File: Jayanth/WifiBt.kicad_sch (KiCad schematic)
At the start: 34 parts, among them J1 Bus_M.2_1-2199230-6, J3 Bus_M.2_2199230-6, Y2 Oscillator_32.768kHz_ECS_2520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

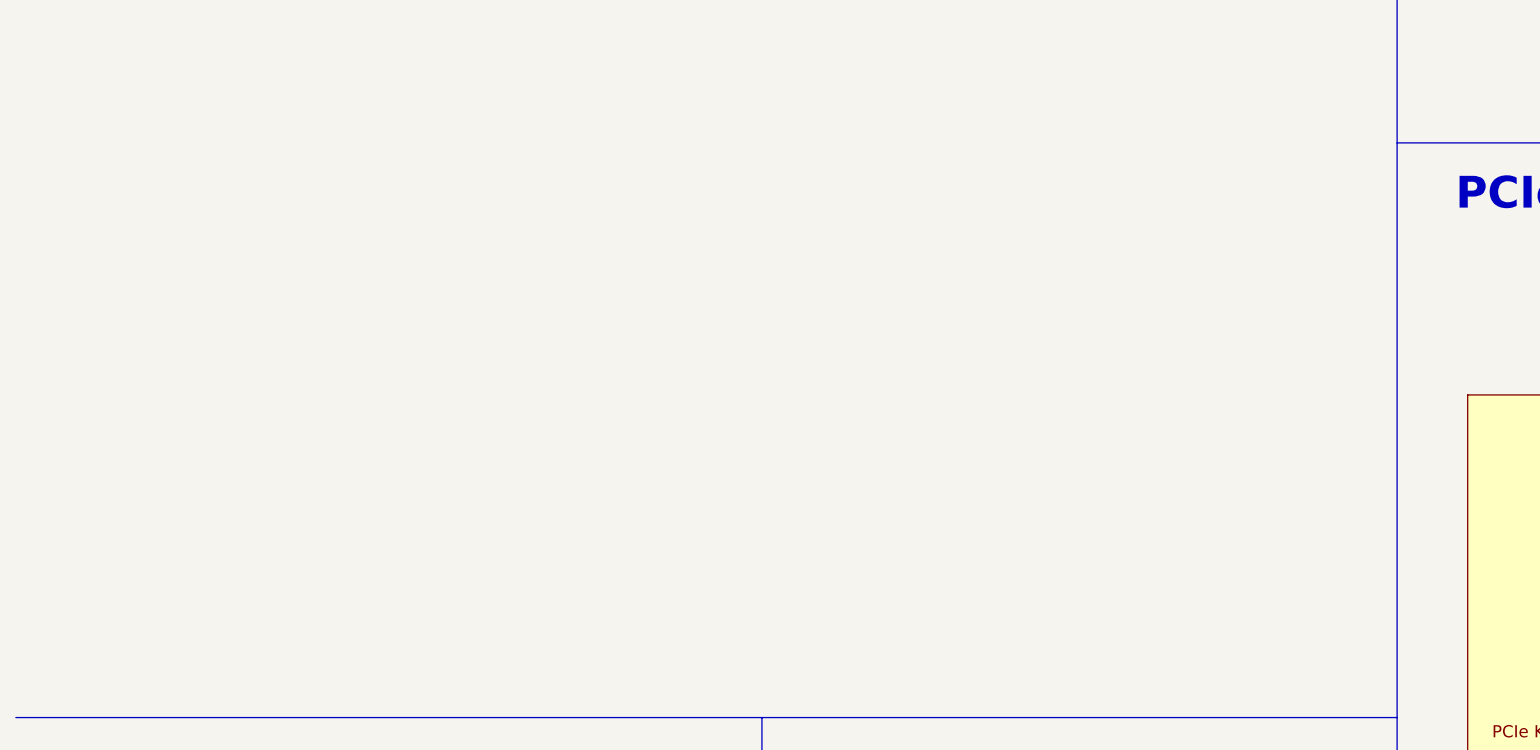
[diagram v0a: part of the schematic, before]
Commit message: added can circuit
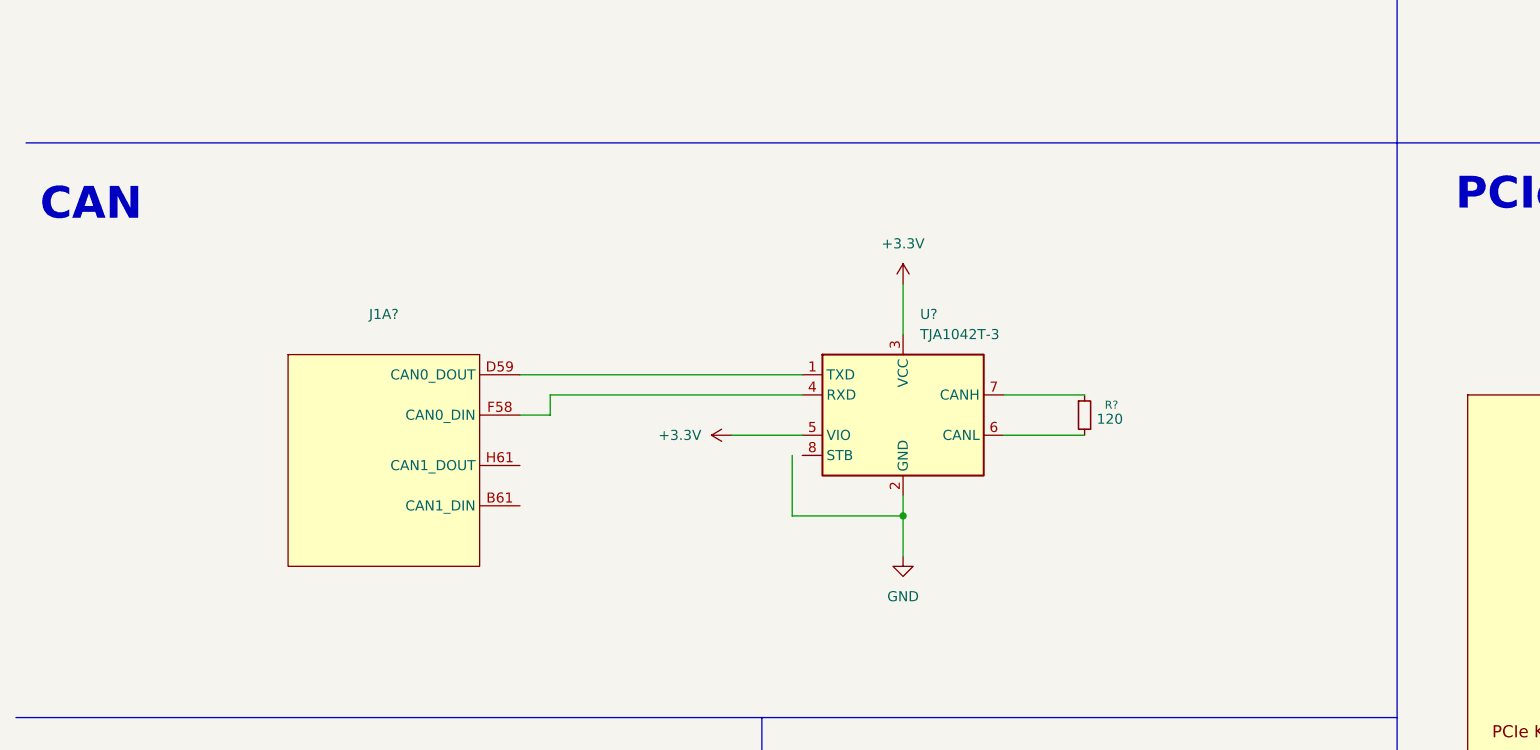
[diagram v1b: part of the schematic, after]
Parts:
- added J1A?: ~, symbol Humanoid:J1_A
- added R?: 120, symbol Device:R_Small
- added U?: TJA1042T-3, Package_SO:SOIC-8_3.9x4.9mm_P1.27mm, symbol Interface_CAN_LIN:TJA1042T-3
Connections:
- net GND: now also U?.2 (GND)
- new net: J1A?.D59 (CAN0_DOUT), U?.1 (TXD)
- new net: J1A?.F58 (CAN0_DIN), U?.4 (RXD)
- new net: R?.1, U?.7 (CANH)
- new net: R?.2, U?.6 (CANL)
- new net +3.3V: U?.3 (VCC), U?.5 (VIO)
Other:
- note added: "CAN"

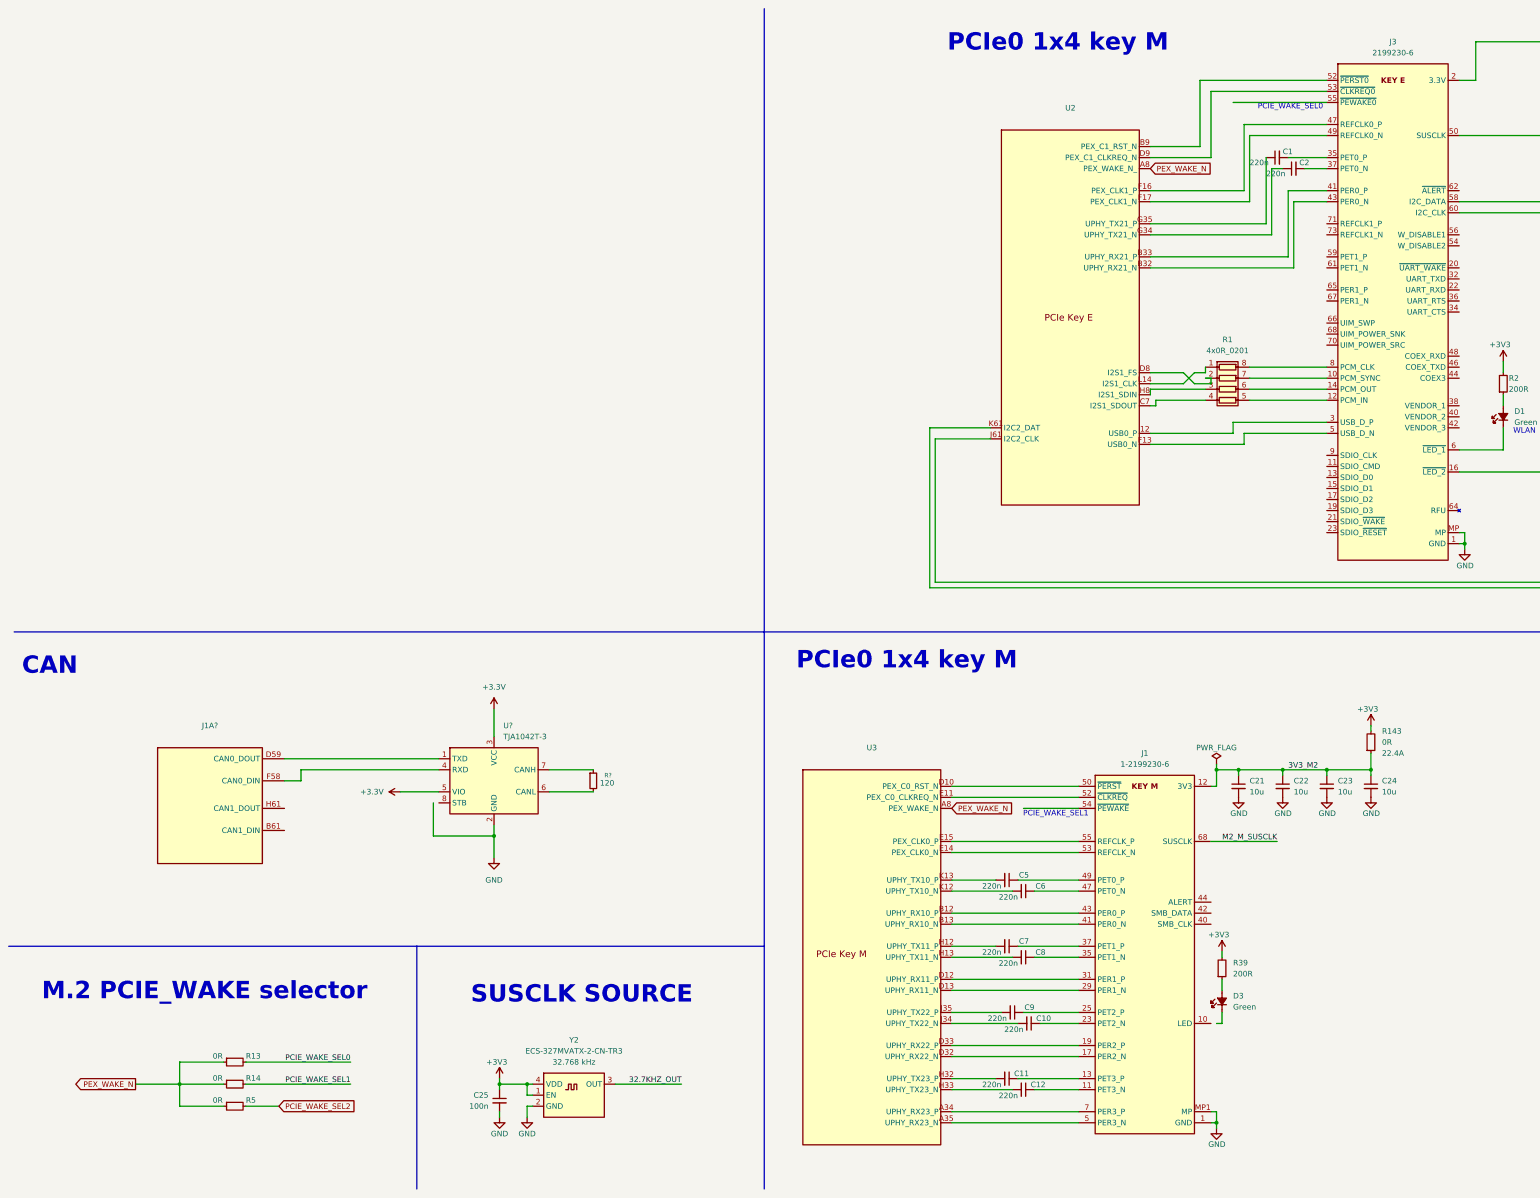
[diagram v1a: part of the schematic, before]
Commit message: added fan ctrl
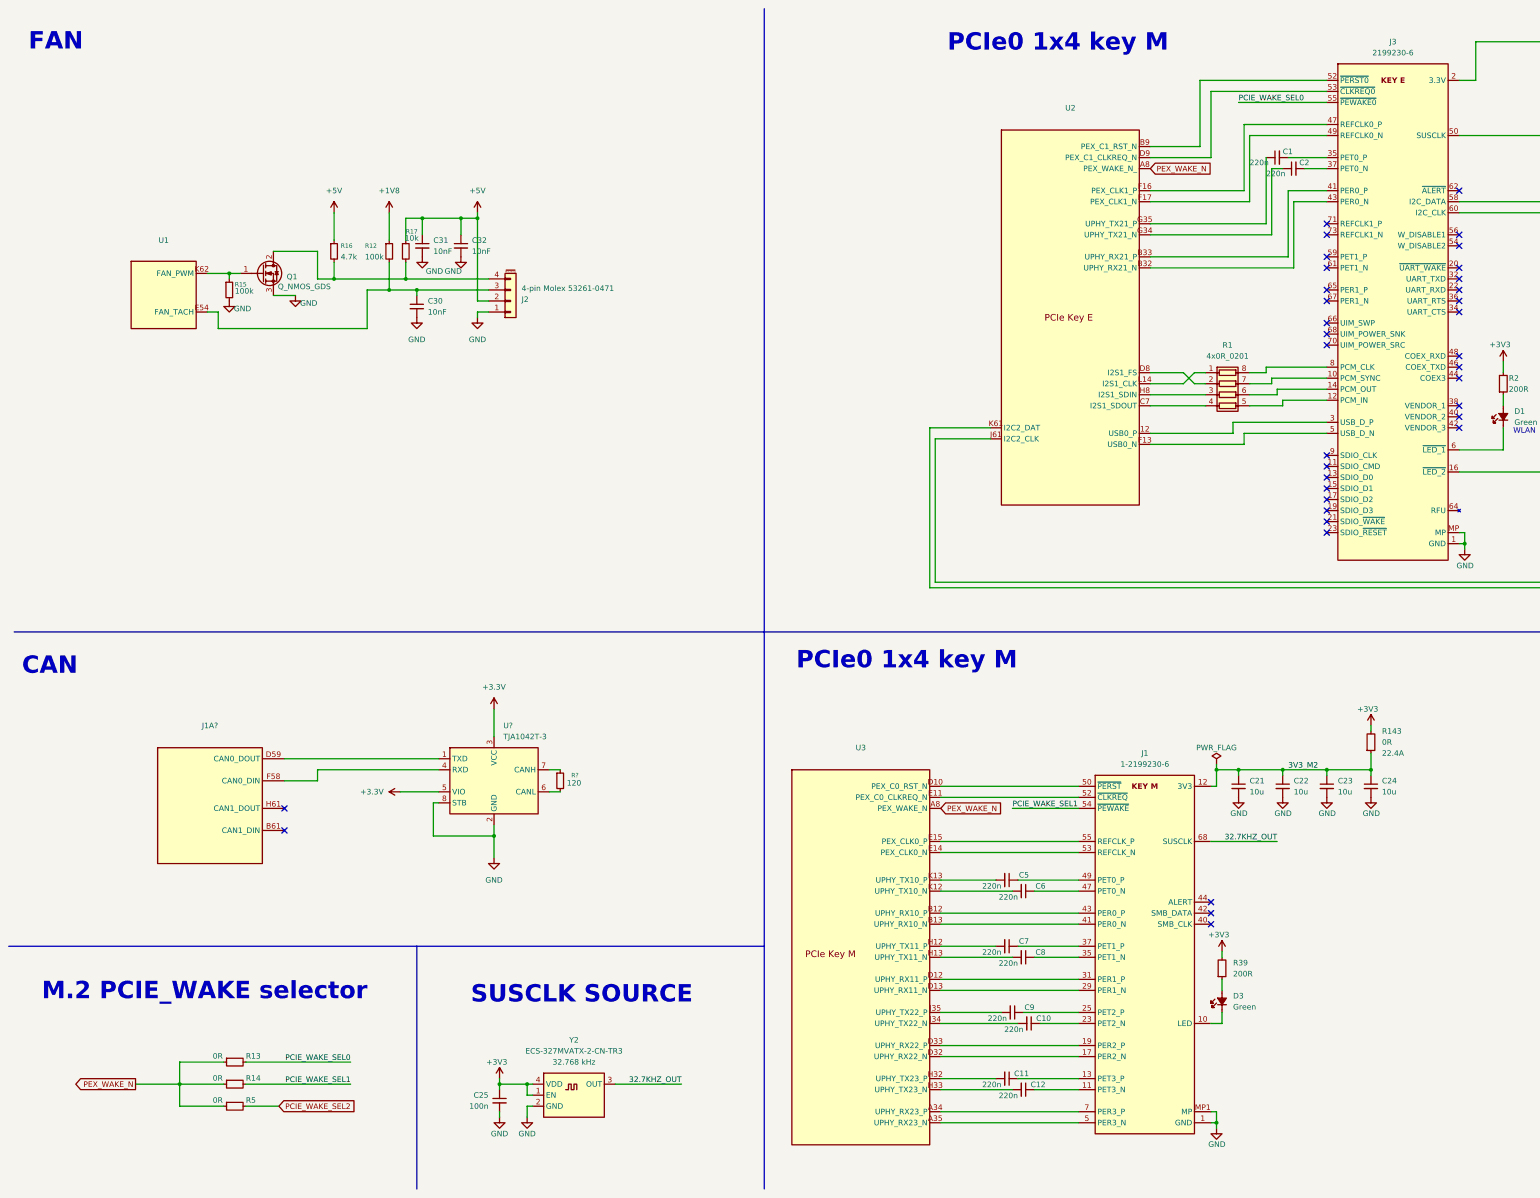
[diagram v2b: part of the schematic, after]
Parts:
- added C30, C31, C32: 10nF, symbol Device:C_Small
- added J2: 4-pin Molex 53261-0471, symbol Connector_Generic_MountingPin:Conn_01x04_MountingPin
- added Q1: Q_NMOS_GDS, symbol Transistor_FET:Q_NMOS_GDS
- added R12, R15: 100k, symbol Device:R_Small
- added R16: 4.7k, symbol Device:R_Small
- added R17: 10k, symbol Device:R_Small
- added U1: ~, symbol Jetson_orin:FanCtrl
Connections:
- net M2_M_SUSCLK is gone; now on net 32.7KHZ_OUT: J1.68 (SUSCLK)
- net GND: now also U?.8 (STB), C30.2, C31.2, C32.2, J2.1 (Pin_1), Q1.3 (S), R15.2
- net PCIE_WAKE_SEL0: now also J3.55 (~{PEWAKE0})
- net PCIE_WAKE_SEL1: now also J1.54 (~{PEWAKE})
- net at D3.1 (C): now also J1.10 (LED)
- new net: J2.4 (Pin_4), Q1.2 (D), R16.2, R17.2
- new net: C30.1, J2.3 (Pin_3), R12.2, U1.E54 (FAN_TACH)
- new net: Q1.1 (G), R15.1, U1.K62 (FAN_PWM)
- new net +1V8: R12.1
- new net +5V: C31.1, C32.1, J2.2 (Pin_2), R16.1, R17.1
- no-connect marks 0 -> 36
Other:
- note added: "FAN"
- note removed: "PCIE_WAKE_SEL0"
- note removed: "PCIE_WAKE_SEL1"
- moved on the sheet: R1, R?, U3
